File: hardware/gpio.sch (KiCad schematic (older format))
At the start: 18 parts, among them T1 BUZ11, T2 BUZ11, U7 SN74LVC1G14, U8 SN74LVC1G14

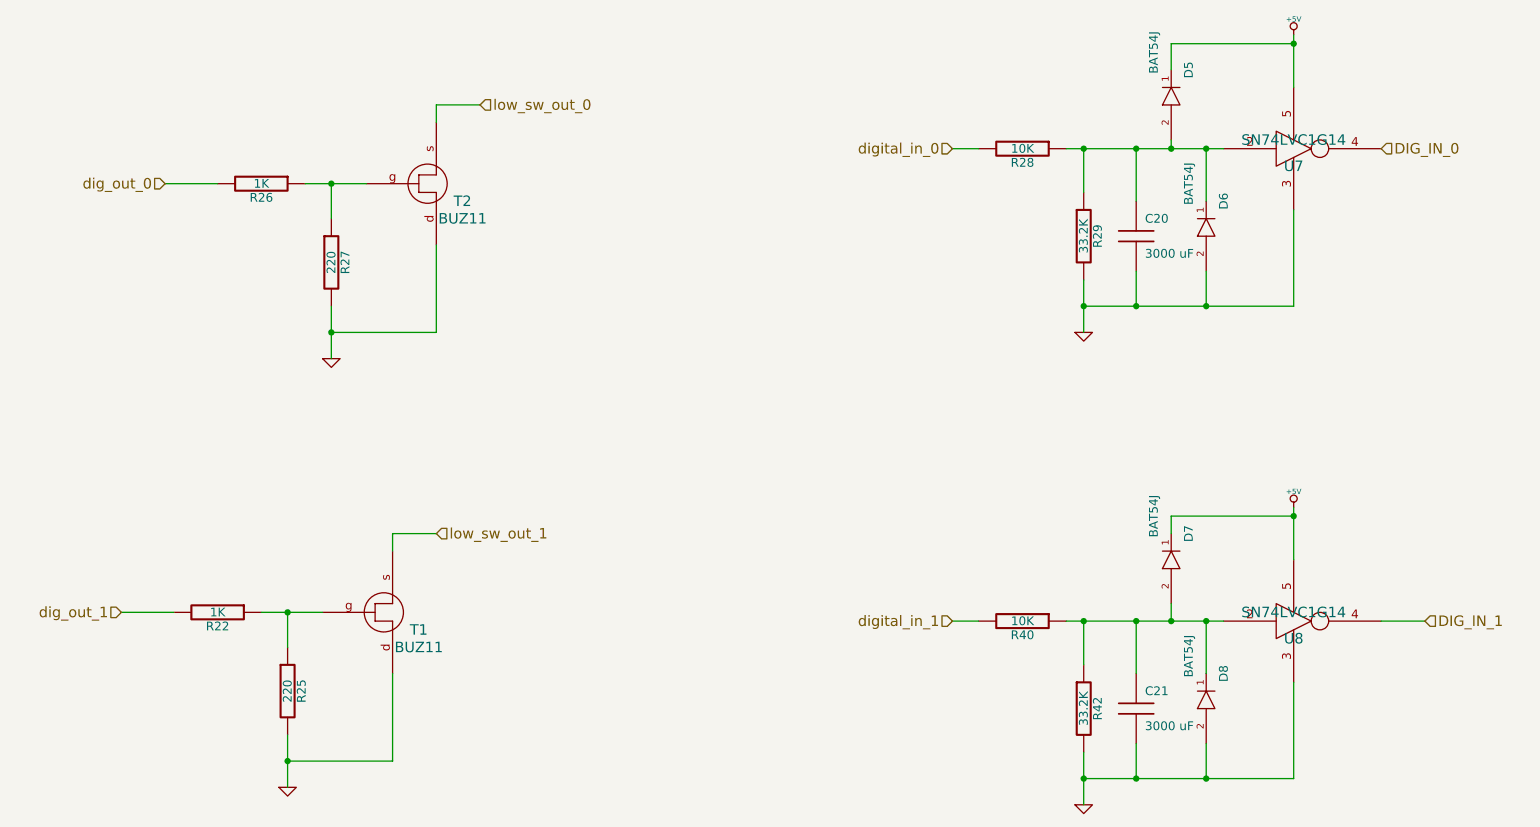
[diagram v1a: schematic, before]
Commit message: fixed some ERCs and simplified reset
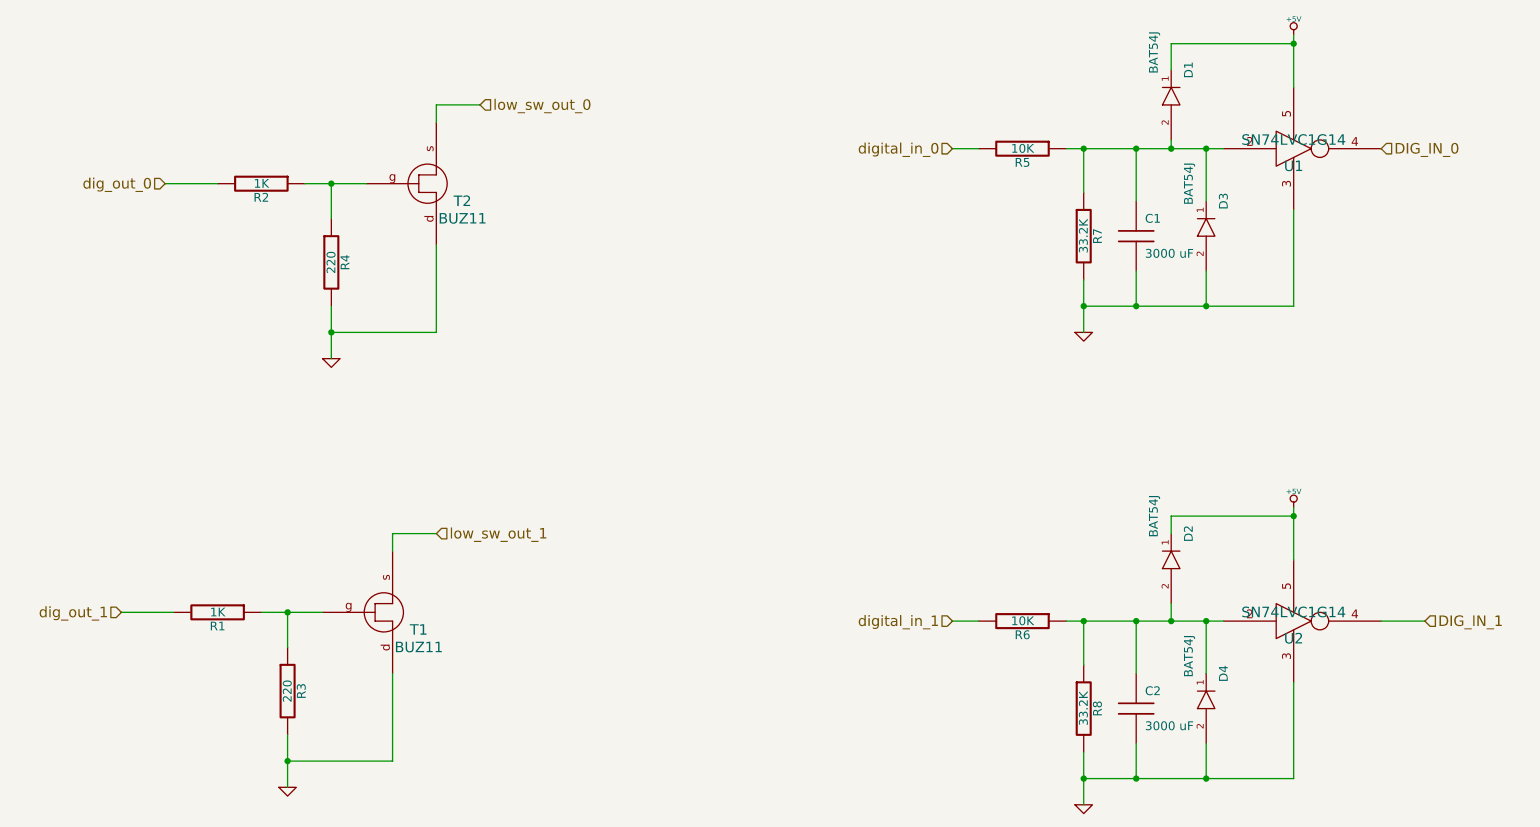
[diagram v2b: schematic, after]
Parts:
- renumbered C20 to C1, C21 to C2, D5 to D1, D7 to D2, D6 to D3, D8 to D4, R22 to R1, R26 to R2, R25 to R3, R27 to R4, R28 to R5, R40 to R6, R29 to R7, R42 to R8, U7 to U1, U8 to U2
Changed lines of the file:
@@
-EESchema Schematic File Version 2  date Sat 26 Apr 2014 10:24:32 PM EDT
+EESchema Schematic File Version 2  date Wed 30 Apr 2014 02:36:15 PM EDT
 LIBS:power
 LIBS:device
@@
 Sheet 2 6
 Title ""
-Date "27 apr 2014"
+Date "30 apr 2014"
 Rev ""
 Comp ""
@@
 Connection ~ 8350 5750
 Wire Wire Line
-	8350 5550 8350 5750
+	8350 5750 8350 5550
 Connection ~ 8850 4250
 Wire Wire Line
@@
 	7050 2150 6900 2150
 Wire Wire Line
-	8850 4500 8850 4250
-Wire Wire Line
-	8850 4250 8850 4200
+	8850 4500 8850 4200
 Connection ~ 7950 4850
 Wire Wire Line
-	7950 5150 7950 4850
-Wire Wire Line
-	7550 4850 7650 4850
-Wire Wire Line
-	7650 4850 7950 4850
-Wire Wire Line
-	7950 4850 8150 4850
-Wire Wire Line
-	8150 4850 8350 4850
-Wire Wire Line
-	8350 4850 8450 4850
+	7950 4850 7950 5150
+Wire Wire Line
+	7550 4850 8450 4850
 Connection ~ 7950 5750
 Wire Wire Line
-	7650 5750 7950 5750
-Wire Wire Line
-	7950 5750 8350 5750
-Wire Wire Line
-	8350 5750 8850 5750
+	7650 5750 8850 5750
 Wire Wire Line
 	8850 5750 8850 5200
 Wire Wire Line
-	7650 5600 7650 5750
-Wire Wire Line
-	7650 5750 7650 5900
+	7650 5600 7650 5900
 Wire Wire Line
 	7950 5750 7950 5550
@@
 	3700 4350 3950 4350
 Wire Wire Line
-	3100 5500 3100 5650
-Wire Wire Line
-	3100 5650 3100 5800
-Wire Wire Line
-	3300 4800 3100 4800
-Wire Wire Line
-	3100 4800 2950 4800
+	3100 5500 3100 5800
+Wire Wire Line
+	3300 4800 2950 4800
 Wire Wire Line
 	2450 4800 2150 4800
@@
 	2700 2350 2400 2350
 Wire Wire Line
-	3550 2350 3350 2350
-Wire Wire Line
-	3350 2350 3200 2350
-Wire Wire Line
-	3350 3050 3350 3200
-Wire Wire Line
-	3350 3200 3350 3350
+	3550 2350 3200 2350
+Wire Wire Line
+	3350 3050 3350 3350
 Wire Wire Line
 	4200 1900 3950 1900
@@
 Connection ~ 3350 2350
 Wire Wire Line
-	7650 2900 7650 3050
-Wire Wire Line
-	7650 3050 7650 3200
+	7650 2900 7650 3200
 Wire Wire Line
 	8850 2500 8850 3050
 Wire Wire Line
-	8850 3050 8350 3050
-Wire Wire Line
-	8350 3050 7950 3050
-Wire Wire Line
-	7950 3050 7650 3050
+	8850 3050 7650 3050
 Connection ~ 7950 3050
 Wire Wire Line
-	7550 2150 7650 2150
-Wire Wire Line
-	7650 2150 7950 2150
-Wire Wire Line
-	7950 2150 8150 2150
-Wire Wire Line
-	8150 2150 8350 2150
-Wire Wire Line
-	8350 2150 8450 2150
+	7550 2150 8450 2150
 Wire Wire Line
 	7950 2150 7950 2450
 Connection ~ 7950 2150
 Wire Wire Line
-	8850 1800 8850 1550
-Wire Wire Line
-	8850 1550 8850 1500
+	8850 1800 8850 1500
 Wire Wire Line
 	7050 4850 6900 4850
@@
 Connection ~ 8350 4850
 $Comp
-L BAT54J D8
+L BAT54J D4
 U 1 1 526D729D
 P 8350 5350
-F 0 "D8" H 8550 5250 50  0000 C CNN
+F 0 "D4" H 8550 5250 50  0000 C CNN
 F 1 "BAT54J" H 8650 5450 50  0000 C CNN
 F 2 "1206" H 8360 5450 30  0001 C CNN
@@
 $EndComp
 $Comp
-L BAT54J D7
+L BAT54J D2
 U 1 1 526D7261
 P 8150 4550
-F 0 "D7" H 8350 4450 50  0000 C CNN
+F 0 "D2" H 8350 4450 50  0000 C CNN
 F 1 "BAT54J" H 8450 4650 50  0000 C CNN
 F 2 "1206" H 8160 4650 30  0001 C CNN
@@
 $EndComp
 $Comp
-L BAT54J D5
+L BAT54J D1
 U 1 1 526D7217
 P 8150 1900
-F 0 "D5" H 8350 1800 50  0000 C CNN
+F 0 "D1" H 8350 1800 50  0000 C CNN
 F 1 "BAT54J" H 8450 2000 50  0000 C CNN
 F 2 "1206" H 8160 2000 30  0001 C CNN
@@
 $EndComp
 $Comp
-L BAT54J D6
+L BAT54J D3
 U 1 1 526D7182
 P 8350 2650
-F 0 "D6" H 8550 2550 50  0000 C CNN
+F 0 "D3" H 8550 2550 50  0000 C CNN
 F 1 "BAT54J" H 8650 2750 50  0000 C CNN
 F 2 "1206" H 8360 2750 30  0001 C CNN
@@
 digital_in_0
 $Comp
-L SN74LVC1G14 U8
+L SN74LVC1G14 U2
 U 1 1 526D6DA2
 P 8850 4850
-F 0 "U8" H 8850 4750 60  0000 C CNN
+F 0 "U2" H 8850 4750 60  0000 C CNN
 F 1 "SN74LVC1G14" H 8850 4900 60  0000 C CNN
 	1    8850 4850
@@
 DIG_IN_1
 $Comp
-L R R42
+L R R8
 U 1 1 526D6DA1
 P 7650 5350
-F 0 "R42" V 7730 5350 50  0000 C CNN
+F 0 "R8" V 7730 5350 50  0000 C CNN
 F 1 "33.2K" V 7650 5350 50  0000 C CNN
 	1    7650 5350
@@
 $EndComp
 $Comp
-L C C21
+L C C2
 U 1 1 526D6DA0
 P 7950 5350
-F 0 "C21" H 8000 5450 50  0000 L CNN
+F 0 "C2" H 8000 5450 50  0000 L CNN
 F 1 "3000 uF" H 8000 5250 50  0000 L CNN
 	1    7950 5350
@@
 $EndComp
 $Comp
-L R R40
+L R R6
 U 1 1 526D6D9F
 P 7300 4850
-F 0 "R40" V 7380 4850 50  0000 C CNN
+F 0 "R6" V 7380 4850 50  0000 C CNN
 F 1 "10K" V 7300 4850 50  0000 C CNN
 	1    7300 4850
@@
 $EndComp
 $Comp
-L GND #PWR025
+L GND #PWR01
 U 1 1 526D6D9E
 P 7650 5900
-F 0 "#PWR025" H 7650 5900 30  0001 C CNN
+F 0 "#PWR01" H 7650 5900 30  0001 C CNN
 F 1 "GND" H 7650 5830 30  0001 C CNN
 	1    7650 5900
@@
 $EndComp
 $Comp
-L +5V #PWR026
+L +5V #PWR02
 U 1 1 526D6D9D
 P 8850 4200
-F 0 "#PWR026" H 8850 4290 20  0001 C CNN
+F 0 "#PWR02" H 8850 4290 20  0001 C CNN
 F 1 "+5V" H 8850 4290 30  0000 C CNN
 	1    8850 4200
@@
 $EndComp
 $Comp
-L +5V #PWR027
+L +5V #PWR03
 U 1 1 526D6C72
 P 8850 1500
-F 0 "#PWR027" H 8850 1590 20  0001 C CNN
+F 0 "#PWR03" H 8850 1590 20  0001 C CNN
 F 1 "+5V" H 8850 1590 30  0000 C CNN
 	1    8850 1500
@@
 $EndComp
 $Comp
-L GND #PWR028
+L GND #PWR04
 U 1 1 526D6C43
 P 7650 3200
-F 0 "#PWR028" H 7650 3200 30  0001 C CNN
+F 0 "#PWR04" H 7650 3200 30  0001 C CNN
 F 1 "GND" H 7650 3130 30  0001 C CNN
 	1    7650 3200
@@
 $EndComp
 $Comp
-L R R28
+L R R5
 U 1 1 526D6C1B
 P 7300 2150
-F 0 "R28" V 7380 2150 50  0000 C CNN
+F 0 "R5" V 7380 2150 50  0000 C CNN
 F 1 "10K" V 7300 2150 50  0000 C CNN
 	1    7300 2150
@@
 $EndComp
 $Comp
-L GND #PWR029
+L GND #PWR05
 U 1 1 526D6AE7
 P 3100 5800
-F 0 "#PWR029" H 3100 5800 30  0001 C CNN
+F 0 "#PWR05" H 3100 5800 30  0001 C CNN
 F 1 "GND" H 3100 5730 30  0001 C CNN
 	1    3100 5800
@@
 $EndComp
 $Comp
-L R R22
+L R R1
 U 1 1 526D6AE5
 P 2700 4800
-F 0 "R22" V 2780 4800 50  0000 C CNN
+F 0 "R1" V 2780 4800 50  0000 C CNN
 F 1 "1K" V 2700 4800 50  0000 C CNN
 	1    2700 4800
@@
 $EndComp
 $Comp
-L R R25
+L R R3
 U 1 1 526D6AE4
 P 3100 5250
-F 0 "R25" V 3180 5250 50  0000 C CNN
+F 0 "R3" V 3180 5250 50  0000 C CNN
 F 1 "220" V 3100 5250 50  0000 C CNN
 	1    3100 5250
@@
 low_sw_out_0
 $Comp
-L R R27
+L R R4
 U 1 1 526D69D9
 P 3350 2800
-F 0 "R27" V 3430 2800 50  0000 C CNN
+F 0 "R4" V 3430 2800 50  0000 C CNN
 F 1 "220" V 3350 2800 50  0000 C CNN
 	1    3350 2800
@@
 $EndComp
 $Comp
-L R R26
+L R R2
 U 1 1 526D69CD
 P 2950 2350
-F 0 "R26" V 3030 2350 50  0000 C CNN
+F 0 "R2" V 3030 2350 50  0000 C CNN
 F 1 "1K" V 2950 2350 50  0000 C CNN
 	1    2950 2350
@@
 $EndComp
 $Comp
-L C C20
+L C C1
 U 1 1 5265748E
 P 7950 2650
-F 0 "C20" H 8000 2750 50  0000 L CNN
+F 0 "C1" H 8000 2750 50  0000 L CNN
 F 1 "3000 uF" H 8000 2550 50  0000 L CNN
 	1    7950 2650
@@
 $EndComp
 $Comp
-L R R29
+L R R7
 U 1 1 52657472
 P 7650 2650
-F 0 "R29" V 7730 2650 50  0000 C CNN
+F 0 "R7" V 7730 2650 50  0000 C CNN
 F 1 "33.2K" V 7650 2650 50  0000 C CNN
 	1    7650 2650
@@
 DIG_IN_0
 $Comp
-L GND #PWR030
+L GND #PWR06
 U 1 1 5265735B
 P 3350 3350
-F 0 "#PWR030" H 3350 3350 30  0001 C CNN
+F 0 "#PWR06" H 3350 3350 30  0001 C CNN
 F 1 "GND" H 3350 3280 30  0001 C CNN
 	1    3350 3350
@@
 $EndComp
 $Comp
-L SN74LVC1G14 U7
+L SN74LVC1G14 U1
 U 1 1 526572BC
 P 8850 2150
-F 0 "U7" H 8850 2050 60  0000 C CNN
+F 0 "U1" H 8850 2050 60  0000 C CNN
 F 1 "SN74LVC1G14" H 8850 2200 60  0000 C CNN
 	1    8850 2150
